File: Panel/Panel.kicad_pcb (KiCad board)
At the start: 2 copper layers, 70.8 x 128.5 mm, 32 parts

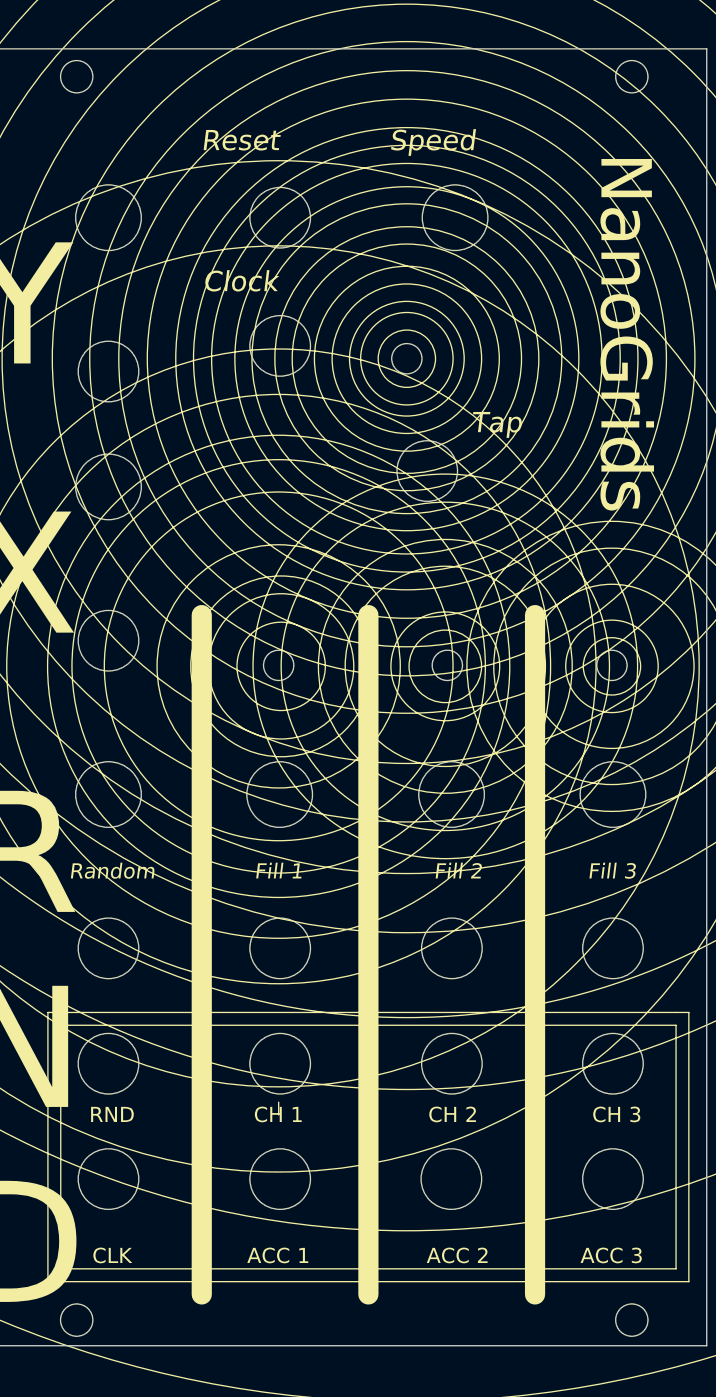
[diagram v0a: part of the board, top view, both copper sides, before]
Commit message: Panel
Bigger holes for pots
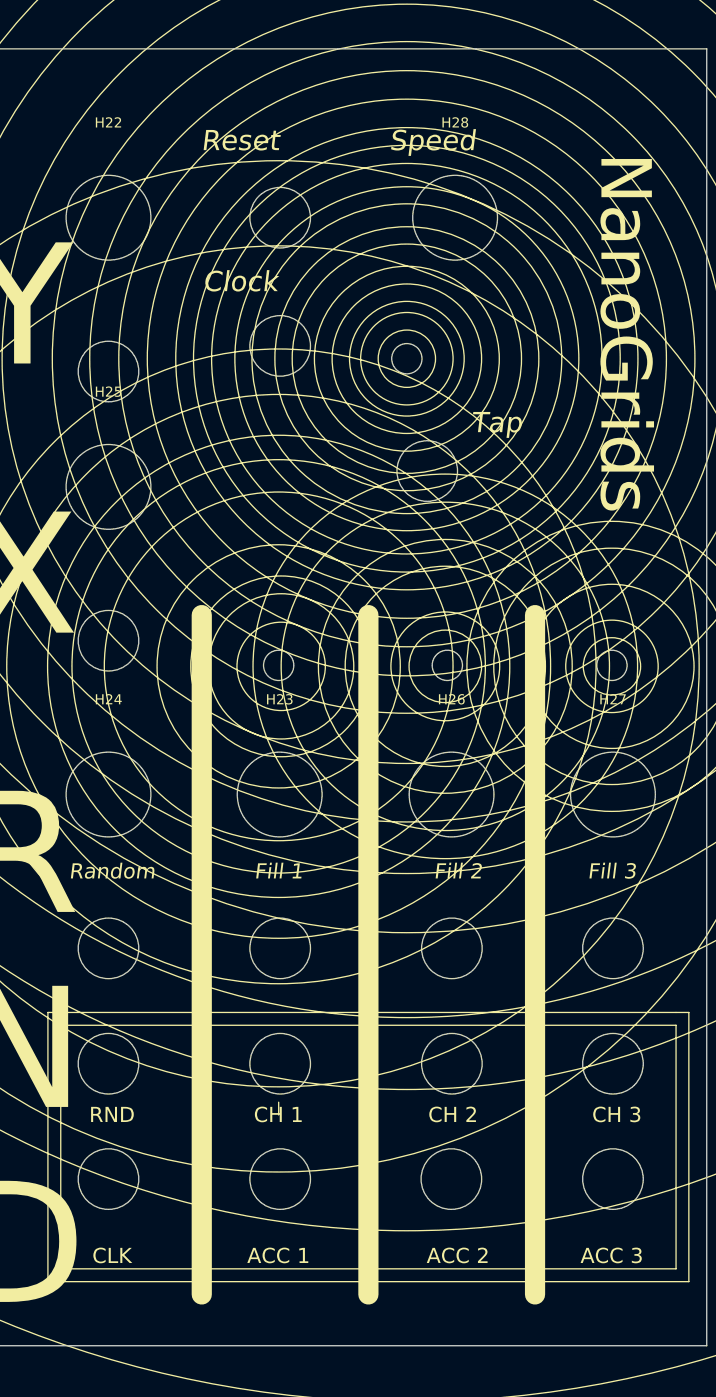
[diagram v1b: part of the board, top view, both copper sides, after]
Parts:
- removed REF** (x4): MountingHole_3.2mm_M3, MountingHole:MountingHole_3.2mm_M3
- H22, H23, H24, H25, H26, H27, H28: footprint MountingHole:MountingHole_6.5mm -> MountingHole:MountingHole_8.4mm_M8
